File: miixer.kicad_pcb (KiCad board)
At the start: 2 copper layers, 100 x 100 mm, 30 parts, among them J1 USB_C_Receptacle_USB2.0_16P, J2 Conn_01x10_Pin, SW1 SW_SPST, SW2 SW_SPST, SW3 SW_SPST, SW4 SW_SPST, SW5 SW_SPST, SW6 SW_SPST, SW7 SW_SPST, SW8 SW_SPST, U1 ESP32-C3-WROOM-02, U2 ADS1115IDGS, U3 USBLC6-2SC6, U4 AP2127K-3.3, U5 PCF8574T, U6 TLC59208FIRGYR

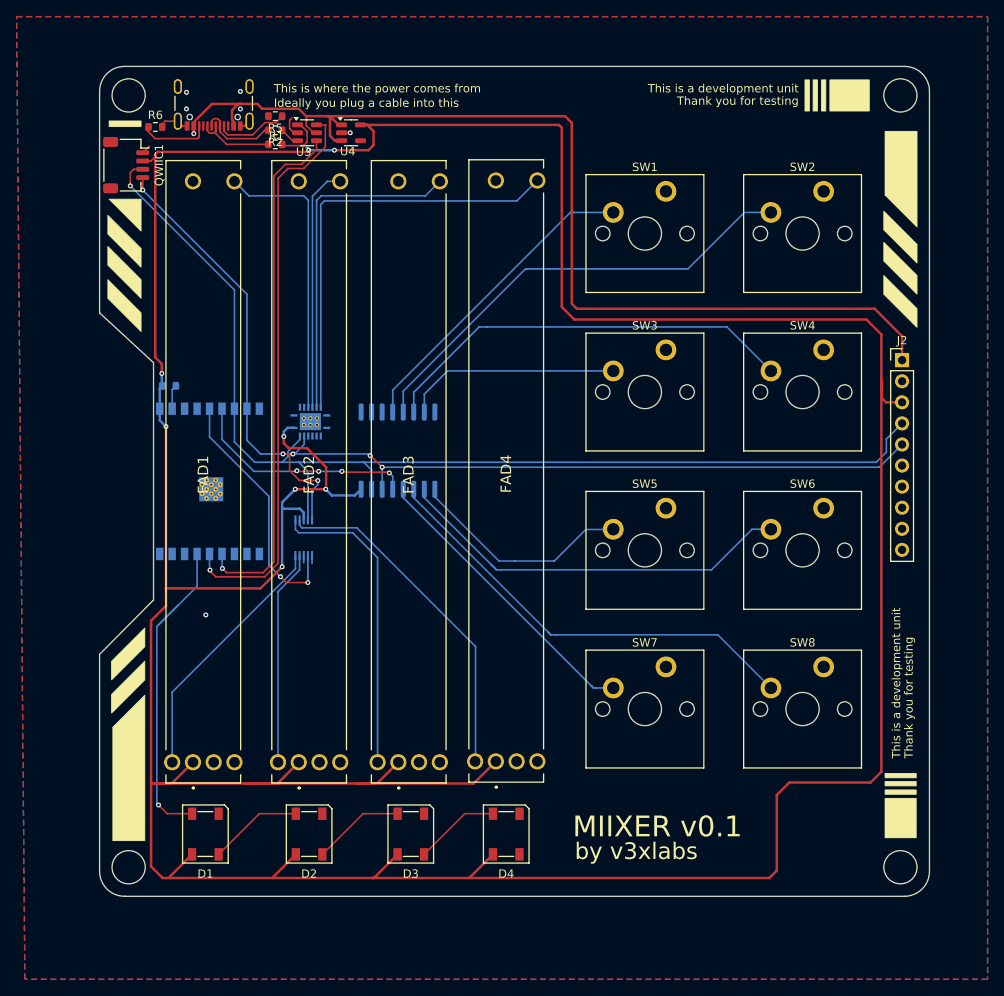
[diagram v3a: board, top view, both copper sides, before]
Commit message: Fix layout, rewiring, and clearances
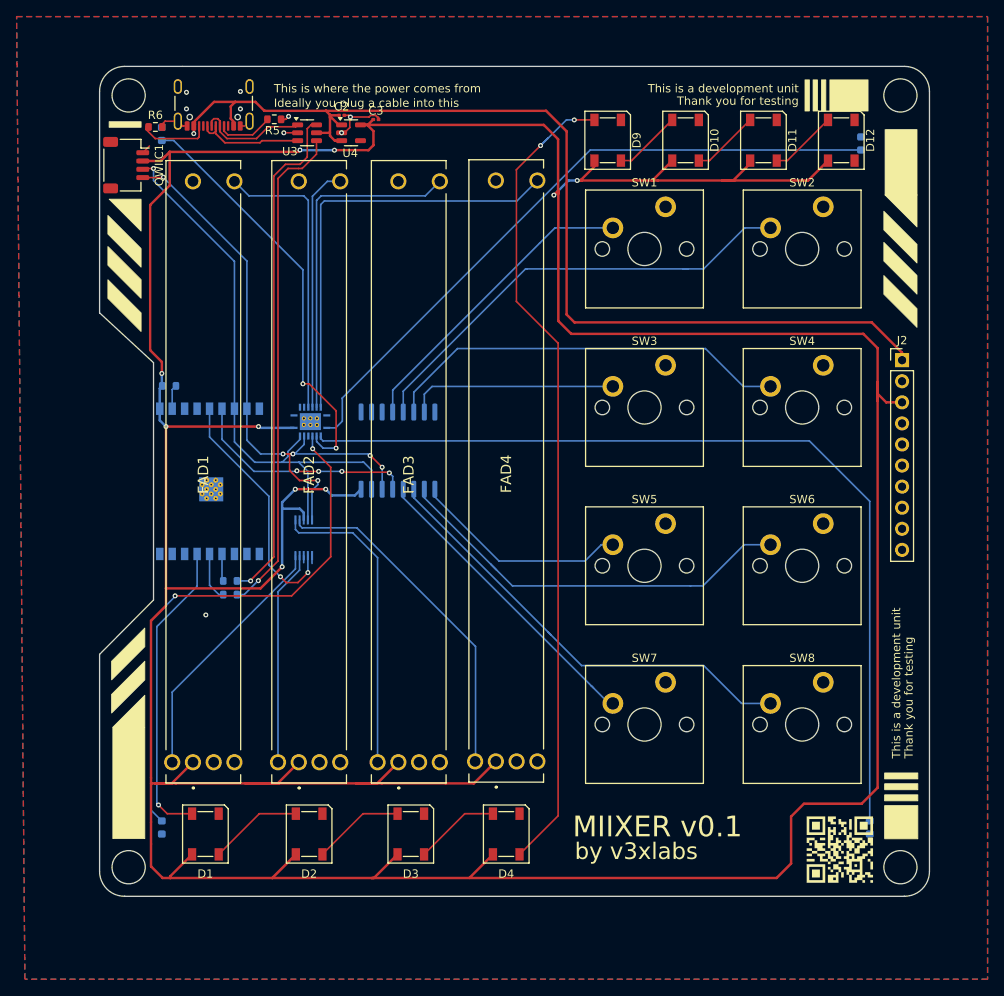
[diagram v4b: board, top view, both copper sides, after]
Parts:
- added C2: C, Capacitor_SMD:C_0201_0603Metric, F.Cu at (58.2, 32.9)
- added C3: C, Capacitor_SMD:C_0201_0603Metric, F.Cu at (62.3, 33.4)
- added D10: SK6812, LED_SMD:LED_SK6812_PLCC4_5.0x5.0mm_P3.2mm, F.Cu at (99.6, 35.9)
- added D11: SK6812, LED_SMD:LED_SK6812_PLCC4_5.0x5.0mm_P3.2mm, F.Cu at (109.0, 35.9)
- added D12: SK6812, LED_SMD:LED_SK6812_PLCC4_5.0x5.0mm_P3.2mm, F.Cu at (118.4, 35.9)
- added D5: LED, LED_SMD:LED_0603_1608Metric, B.Cu at (120.8, 36.3)
- added D6: LED, LED_SMD:LED_0603_1608Metric, B.Cu at (121.8, 118.7)
- added D7: LED, LED_SMD:LED_0603_1608Metric, B.Cu at (36.5, 35.1)
- added D8: LED, LED_SMD:LED_0603_1608Metric, B.Cu at (36.5, 118.7)
- added D9: SK6812, LED_SMD:LED_SK6812_PLCC4_5.0x5.0mm_P3.2mm, F.Cu at (90.2, 35.9)
- added QR*****: miixer_qrcode_0.35px, 00_Luc:miixer_qrcode_0.35px, F.Cu at (118.2, 121.4)
- added QR*****: miixer_qrcode_0.35px, 00_Luc:miixer_qrcode_0.35px, B.Cu at (43.1, 120.0)
- R1, R2: moved to B.Cu
- R4: value R -> 10k
- SW1, SW2, SW3, SW4, SW5, SW6, SW7, SW8: footprint PCM_Switch_Keyboard_Cherry_MX:SW_Cherry_MX_PCB -> PCM_Switch_Keyboard_Cherry_MX:SW_Cherry_MX_PCB_1.00u
- moved R2 54.6 mm to (44.7, 89.0), turned to 0 degrees
- moved R1 54.5 mm to (44.7, 90.7), turned to 0 degrees
- moved SW1 1.86 mm to (94.7, 49.0)
- moved SW2 1.86 mm to (113.7, 49.0)
- moved SW3 1.86 mm to (94.7, 68.1)
- moved SW4 1.86 mm to (113.7, 68.1)
- moved SW5 1.86 mm to (94.7, 87.2)
- moved SW6 1.86 mm to (113.7, 87.2)
- moved SW7 1.86 mm to (94.7, 106.3)
- moved SW8 1.86 mm to (113.7, 106.3)
- moved R5 0.40 mm to (50.0, 33.4), turned to 0 degrees
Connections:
- D4 pad 4: unconnected-(D4-DOUT-Pad4) -> Net-(D4-DOUT)
- J1 pad A6: /USB/USB_D+_RAW -> /USB/USB_RAW_D+
- J1 pad A7: /USB/USB_D-_RAW -> /USB/USB_RAW_D-
- J1 pad B6: /USB/USB_D+_RAW -> /USB/USB_RAW_D+
- J1 pad B7: /USB/USB_D-_RAW -> /USB/USB_RAW_D-
- J2 pad 4: /SDA -> unconnected-(J2-Pin_4-Pad4)
- J2 pad 5: /SCL -> unconnected-(J2-Pin_5-Pad5)
- R1 pad 1: /USB/USB_DP -> /MCU/USBD+
- R1 pad 2: /USB/USB_D+_RAW -> /MCU/USB_D+
- R2 pad 1: /USB/USB_DN -> /MCU/USBD-
- R2 pad 2: /USB/USB_D-_RAW -> /MCU/USB_D-
- U1 pad 13: /MCU/USB_D- -> /MCU/USBD-
- U1 pad 14: /MCU/USB_D+ -> /MCU/USBD+
- U3 pad 1: /USB/USB_DP -> /USB/USB_RAW_D-
- U3 pad 3: /USB/USB_DN -> /USB/USB_RAW_D+
- U3 pad 4: /MCU/USB_D- -> /MCU/USB_D+
- U3 pad 6: /MCU/USB_D+ -> /MCU/USB_D-
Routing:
- net /Buttons/EXTRA_LED_2: track 0.00 -> 108.1 mm
- net Net-(D4-DOUT): track 0.00 -> 99.6 mm, vias 0 -> 2
- net /Buttons/EXTRA_LED_1: track 0.00 -> 79.9 mm
- net /SDA: track 139.0 -> 70.1 mm
- net /Buttons/EXTRA_LED_4: track 0.00 -> 65.1 mm, vias 0 -> 2
- net /SCL: track 134.5 -> 72.3 mm
- net +3.3V: track 489.6 -> 542.6 mm, vias 8 -> 10
- net /Buttons/EXTRA_LED_3: track 0.00 -> 50.4 mm, vias 0 -> 2
- net /USB/USB_RAW_D+: track 0.00 -> 13.8 mm
- net /USB/USB_RAW_D-: track 0.00 -> 13.5 mm
- net /USB/USB_D+_RAW: track 10.2 -> 0.00 mm
- net /USB/USB_D-_RAW: track 9.73 -> 0.00 mm
- net /MCU/USB_D+: track 68.8 -> 60.4 mm
- net Net-(D10-DOUT): track 0.00 -> 8.21 mm
- net Net-(D11-DOUT): track 0.00 -> 8.21 mm
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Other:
- board text added: "If you are reading this."
- board text added: "You might have misoeriented the device"
- board text added: "miixer.v3x.tools"
- board text added: "this is placeholder text"
- board text added: "we thank you for using this product"
- board text added: "you lost the game."

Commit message: Update layout & ground vias
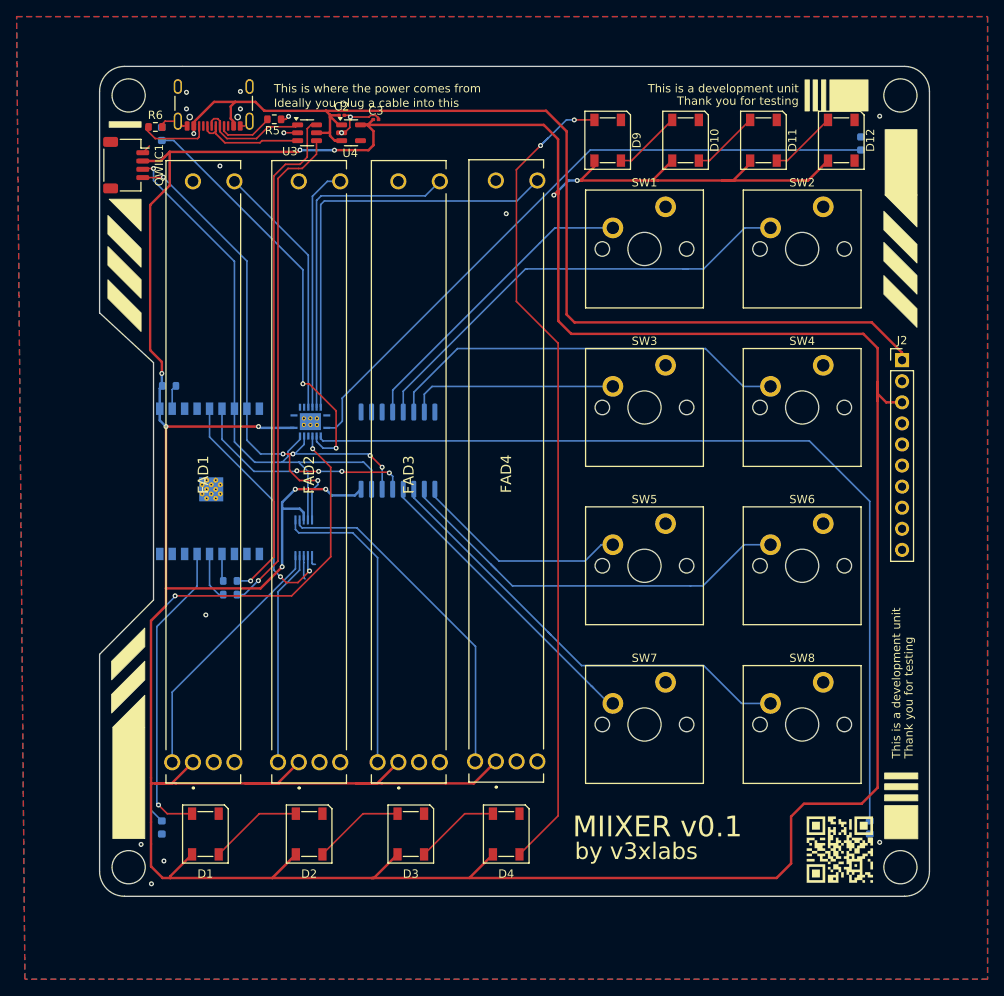
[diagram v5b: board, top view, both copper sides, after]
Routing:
- net /Buttons/FAD1_LED: track 34.8 -> 30.9 mm
- net GND: track 17.7 -> 20.1 mm, vias 9 -> 16
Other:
- board text added: "FADERS"
- board text added: "LEDS"
- board text added: "SWITCHES"

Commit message: temp
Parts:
- J1: value USB_C_Receptacle_USB2.0_16P -> TYPE-C 16PIN 2MD(073)
- moved U5 12.3 mm to (77.2, 73.5)
- turned D8 to -90 degrees
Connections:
- D5 pad 1: GND -> /Buttons/EXTRA_LED_1
- D5 pad 2: /Buttons/EXTRA_LED_1 -> Net-(D5-A)
- D6 pad 1: GND -> /Buttons/EXTRA_LED_2
- D6 pad 2: /Buttons/EXTRA_LED_2 -> Net-(D6-A)
- D7 pad 1: GND -> /Buttons/EXTRA_LED_3
- D7 pad 2: /Buttons/EXTRA_LED_3 -> Net-(D7-A)
- D8 pad 1: GND -> /Buttons/EXTRA_LED_4
- D8 pad 2: /Buttons/EXTRA_LED_4 -> Net-(D8-A)
- FAD1 pad B1: /Buttons/FAD1_LED -> Net-(FAD1-B_(+))
- FAD1 pad E1: GND -> /Buttons/FAD1_LED
- FAD2 pad B1: /Buttons/FAD2_LED -> Net-(FAD2-B_(+))
- FAD2 pad E1: GND -> /Buttons/FAD2_LED
- FAD3 pad B1: /Buttons/FAD3_LED -> Net-(FAD3-B_(+))
- FAD3 pad E1: GND -> /Buttons/FAD3_LED
- FAD4 pad B1: /Buttons/FAD4_LED -> Net-(FAD4-B_(+))
- FAD4 pad E1: GND -> /Buttons/FAD4_LED
- U6 pad 17: unconnected-(U6-EPAD-Pad17) -> GND
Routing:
- net /Buttons/BTN_INTERRUPT: track 27.7 -> 40.5 mm
- net Net-(SW5-A): track 26.4 -> 13.9 mm
- net Net-(SW3-A): track 25.3 -> 13.0 mm
- net Net-(SW4-A): track 49.4 -> 37.2 mm
- net +3.3V: track 542.6 -> 554.8 mm
- net Net-(SW6-A): track 50.1 -> 38.6 mm
- net /SDA: track 70.1 -> 81.1 mm
- net /SCL: track 72.3 -> 83.1 mm, vias 6 -> 4
- net Net-(SW2-A): track 55.5 -> 48.3 mm
- net Net-(SW1-A): track 37.3 -> 30.4 mm
- net Net-(SW8-A): track 54.8 -> 48.0 mm
- net Net-(SW7-A): track 36.9 -> 32.6 mm
- net /Buttons/EXTRA_LED_4: track 65.1 -> 63.2 mm
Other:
- board text added: "You might have misoriented the device"
- board text removed: "You might have misoeriented the device"

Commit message: Update routing
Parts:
- moved U2 19.9 mm to (66.2, 99.2)
- moved U6 18.5 mm to (65.7, 84.4), turned to 90 degrees
- moved U3 11.3 mm to (42.8, 36.4), turned to -90 degrees
- moved C2 5.66 mm to (52.6, 32.1)
- moved C3 5.66 mm to (56.7, 32.6)
- moved U4 5.66 mm to (53.7, 34.2)
- moved R1 4.68 mm to (40.8, 88.1), turned to 180 degrees
- moved R2 3.99 mm to (40.8, 89.7), turned to 180 degrees
- moved R6 1.10 mm to (36.5, 33.5), turned to 90 degrees
- moved R5 1.07 mm to (49.0, 33.1), turned to 90 degrees
- moved J1 0.96 mm to (42.8, 29.5)
- moved QWIIC1 0.15 mm to (32.4, 38.9)
- turned D5 to 90 degrees
- turned D6 to -90 degrees
- turned D7 to 90 degrees
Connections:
- U6 pad 12: /Buttons/EXTRA_LED_4 -> /Buttons/EXTRA_LED_1
- U6 pad 4: /Buttons/FAD1_LED -> /Buttons/FAD4_LED
- U6 pad 5: /Buttons/FAD2_LED -> /Buttons/FAD3_LED
- U6 pad 6: /Buttons/FAD3_LED -> /Buttons/FAD2_LED
- U6 pad 7: /Buttons/FAD4_LED -> /Buttons/FAD1_LED
- U6 pad 9: /Buttons/EXTRA_LED_1 -> /Buttons/EXTRA_LED_4
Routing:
- net /SCL: track 83.1 -> 112.1 mm
- net /Buttons/EXTRA_LED_2: track 108.1 -> 83.9 mm, vias 0 -> 4
- net /Buttons/FAD4_WIPER: track 41.8 -> 19.1 mm
- net /SDA: track 81.1 -> 102.7 mm
- net /Buttons/FAD4_LED: track 51.7 -> 31.2 mm, vias 0 -> 2
- net /Buttons/FAD3_WIPER: track 37.1 -> 19.9 mm
- net /Buttons/ADC_INTERRUPT: track 30.1 -> 46.5 mm
- net /Buttons/EXTRA_LED_3: track 50.4 -> 65.8 mm
- net /Buttons/FAD3_LED: track 40.7 -> 26.6 mm, vias 0 -> 2
- net /USB/USB_RAW_D+: track 13.8 -> 4.56 mm
- net /USB/USB_RAW_D-: track 13.5 -> 4.76 mm
- net /Buttons/FAD1_LED: track 30.9 -> 39.4 mm, vias 0 -> 4
- net /Buttons/EXTRA_LED_1: track 79.9 -> 88.1 mm, vias 0 -> 2
- net /Buttons/EXTRA_LED_4: track 63.2 -> 55.6 mm, vias 2 -> 0
- net VBUS: track 127.4 -> 135.0 mm, vias 1 -> 4
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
